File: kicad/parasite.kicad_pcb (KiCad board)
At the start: 2 copper layers, 22 x 126.4 mm, 31 parts, among them Q1 MMBT3906, Q4 Q_Photo_NPN, SW1 B3U-1000P, U1 E73-2G4M08S1C, U2 SHTC3, Y1 32.768kHz

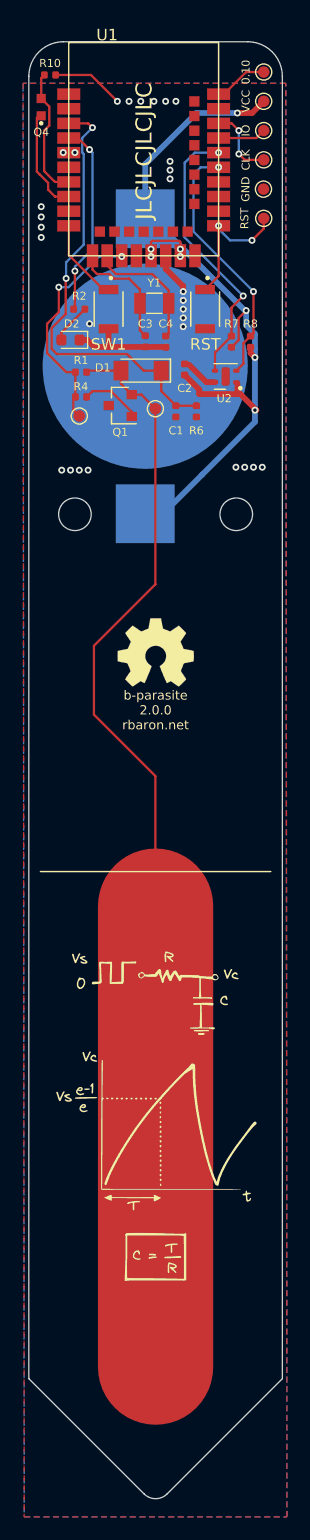
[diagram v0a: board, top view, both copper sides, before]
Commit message: Rounded PCB edges
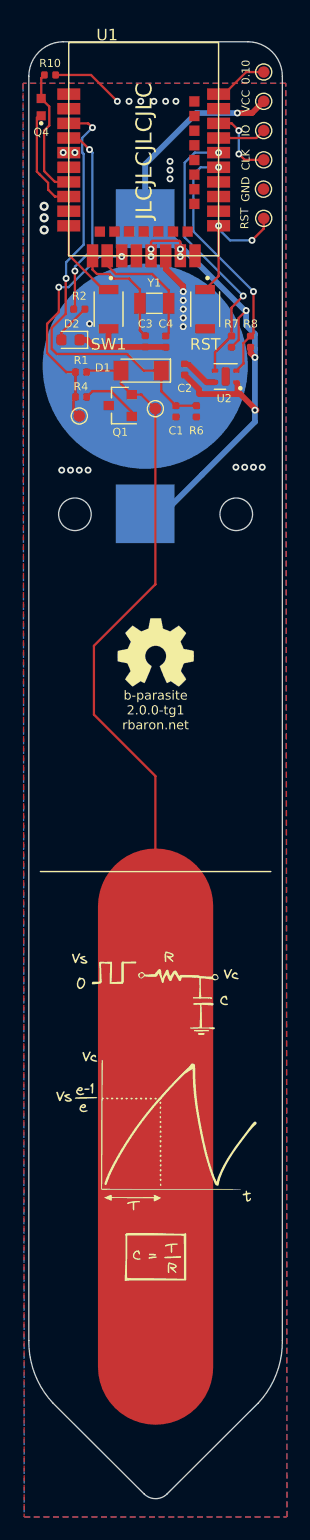
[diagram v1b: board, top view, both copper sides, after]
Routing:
- net GND: vias 29 -> 28
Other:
- outline, holes or cut-outs redrawn
- board text added: "b-parasite 2.0.0-tg1 rbaron.net"
- board text removed: "b-parasite 2.0.0 rbaron.net"
